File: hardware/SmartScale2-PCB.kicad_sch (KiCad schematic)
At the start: 43 parts, among them J1 Conn_ARM_JTAG_SWD_10, J2 USB_C_Receptacle_USB2.0_16P, J3 Conn_01x02, J4 Conn_01x06, J5 Conn_01x03_MountingPin, J6 Conn_01x04_MountingPin, Q1 MMBT4403, SW1 SW_Push_JTP-1130, U1 ESP32-C6-WROOM-1, U2 MCP73831-2-OT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

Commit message: PCB rough layout
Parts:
- removed Q1: MMBT4403, Package_TO_SOT_SMD:SOT-23, symbol Transistor_BJT:Q_PNP_EBC
- added J7: Conn_01x03, symbol Connector_Generic:Conn_01x03
- added Q1: MMBT4403, Package_TO_SOT_SMD:SOT-23, symbol Transistor_BJT:Q_PNP_BEC
- L2: footprint (none) -> Inductor_SMD:L_0805_2012Metric_Pad1.05x1.20mm_HandSolder
- R12: now not fitted
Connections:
- net A+: now also J4.4 (Pin_4); no longer J4.3 (Pin_3)
- net A-: now also J4.3 (Pin_3); no longer J4.4 (Pin_4)
- net B+: now also J4.6 (Pin_6); no longer J4.5 (Pin_5)
- net B-: now also J4.5 (Pin_5); no longer J4.6 (Pin_6)
- net GND: now also J7.1 (Pin_1)
- net T2: now reaches U1.26 (GPIO3/ADC1_CH3)
- net T2: now also J7.2 (Pin_2)
- net T1: now reaches U1.27 (GPIO2/ADC1_CH2)
- net T1: now also J7.3 (Pin_3)
- net Q1_E: now reaches JP1.1 (A), U3.1 (VSUP)
- net Q1_E: now also Q1.2 (E)
- net Q1_B: now reaches U3.2 (BASE)
- net Q1_B: now also Q1.1 (B)
- net Q1_C: now reaches L2.2, R6.1, U3.3 (AVDD)
- net Q1_C: now also Q1.3 (C)

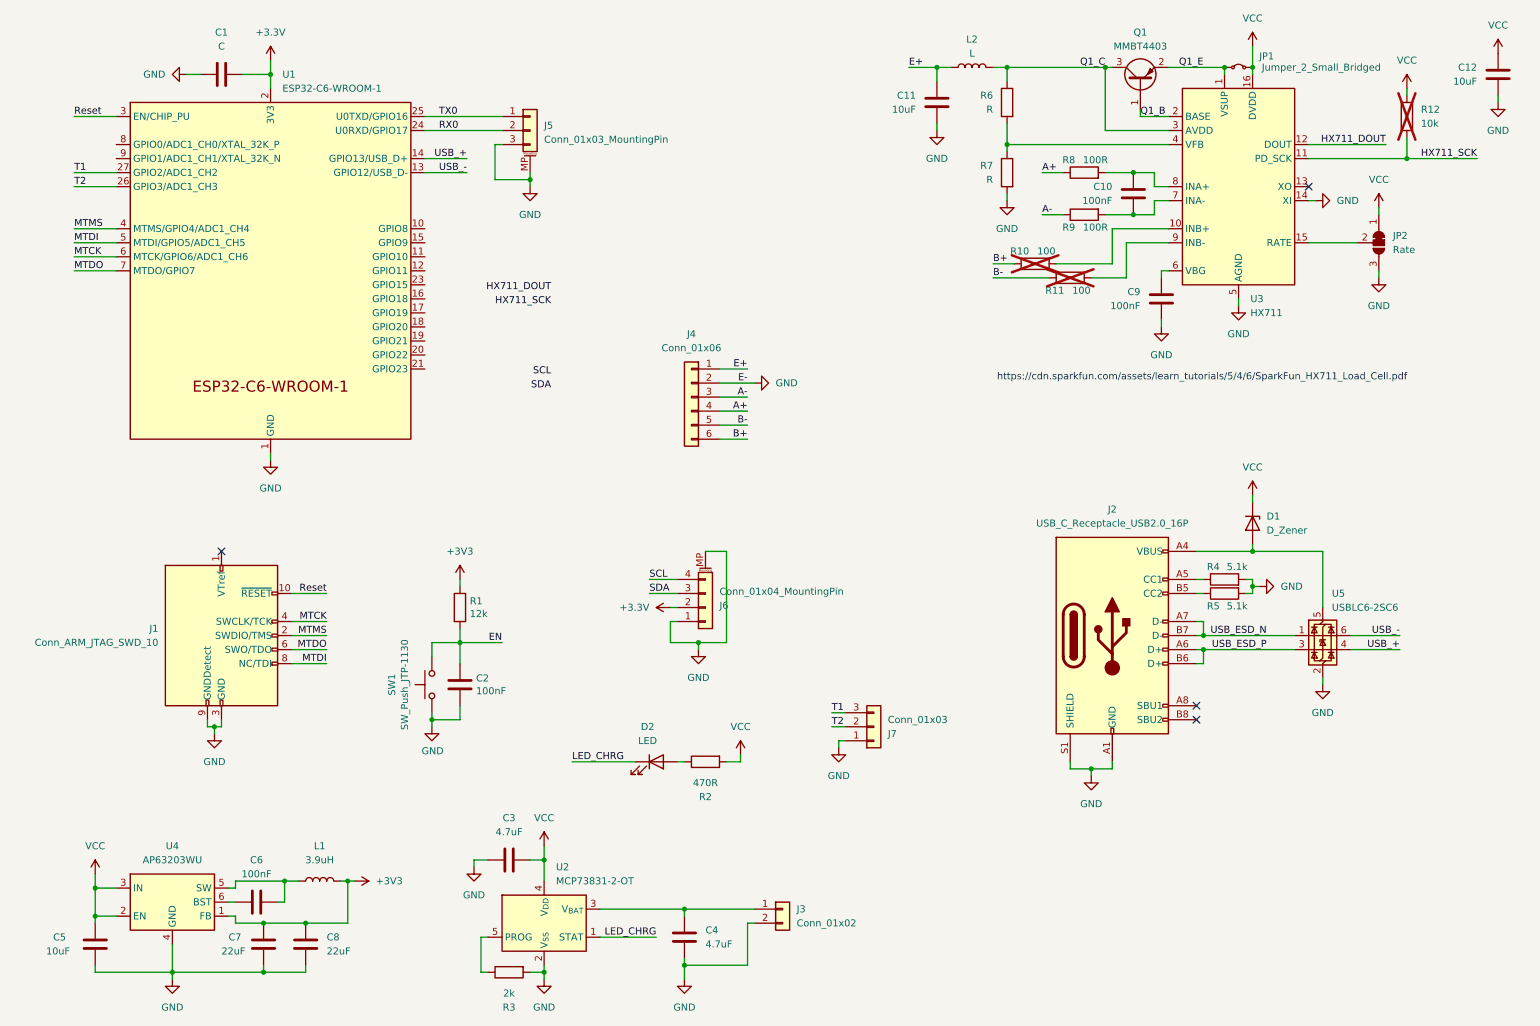
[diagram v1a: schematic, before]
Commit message: Add Touch IC, continue layout
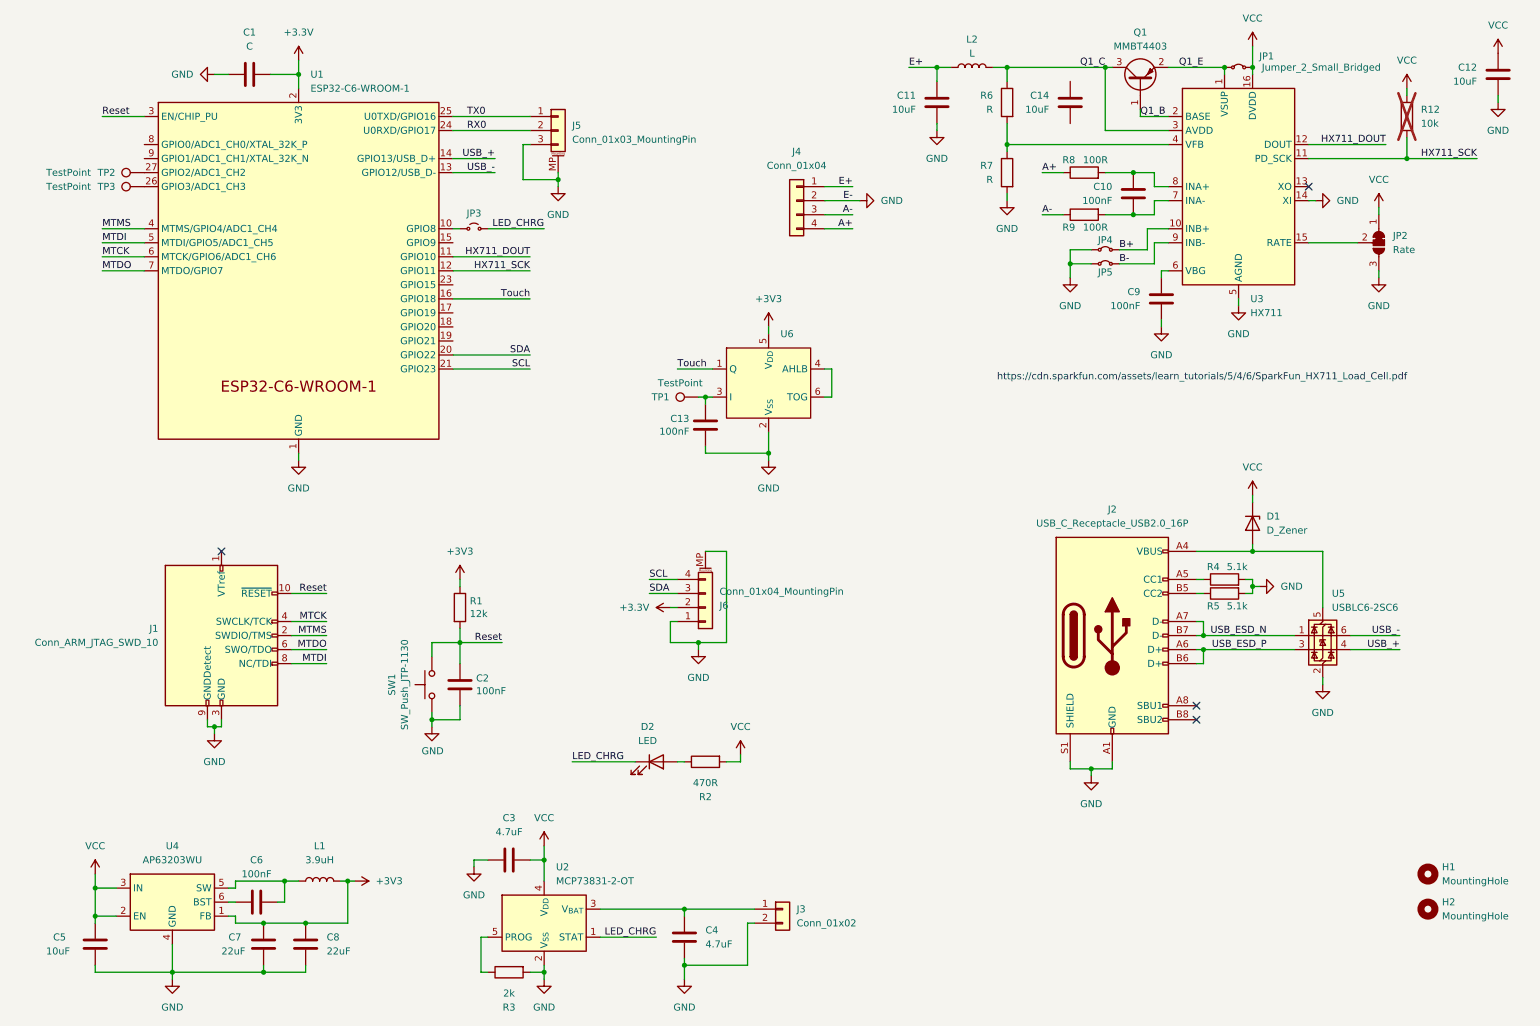
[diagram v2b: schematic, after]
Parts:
- removed J4: Conn_01x06, Connector_PinHeader_2.54mm:PinHeader_1x06_P2.54mm_Vertical, symbol Connector_Generic:Conn_01x06
- removed J7: Conn_01x03, symbol Connector_Generic:Conn_01x03
- removed R10, R11: 100, Resistor_SMD:R_0805_2012Metric_Pad1.20x1.40mm_HandSolder, symbol Device:R
- added C13: 100nF, Capacitor_SMD:C_0805_2012Metric_Pad1.18x1.45mm_HandSolder, symbol SmartScale-rescue:C-Device
- added C14: 10uF, Capacitor_SMD:C_0805_2012Metric_Pad1.18x1.45mm_HandSolder, symbol Device:C
- added H1, H2: MountingHole, MountingHole:MountingHole_3.2mm_M3_DIN965, symbol Mechanical:MountingHole
- added J4: Conn_01x04, Connector_PinSocket_2.54mm:PinSocket_1x04_P2.54mm_Vertical, symbol Connector_Generic:Conn_01x04
- added JP3: Jumper_2_Small_Open, Jumper:SolderJumper-2_P1.3mm_Open_RoundedPad1.0x1.5mm, symbol Jumper:Jumper_2_Small_Open
- added JP4, JP5: Jumper_2_Small_Bridged, Jumper:SolderJumper-2_P1.3mm_Bridged_RoundedPad1.0x1.5mm, symbol Jumper:Jumper_2_Small_Bridged
- added TP1: TestPoint, TestPoint:TestPoint_Loop_D2.50mm_Drill1.0mm, symbol Connector:TestPoint
- added TP2, TP3: TestPoint, TestPoint:TestPoint_Pad_D1.0mm, symbol Connector:TestPoint
- added U6: (no value), Package_TO_SOT_SMD:SOT-23-6, symbol _custom:TTP223-BA6
- D1: footprint (none) -> Diode_SMD:D_SOD-123
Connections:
- net EN is gone; now on net Reset: C2.1, R1.2, SW1.2
- net +3V3: now also U6.5 (V_{DD})
- net A+: now also J4.4 (Pin_4)
- net A-: now also J4.3 (Pin_3)
- net B+: now also U3.10 (INB+), JP4.2 (B)
- net B-: now also U3.9 (INB-), JP5.2 (B)
- net E+: now also J4.1 (Pin_1)
- net GND: now also C13.2, J4.2 (Pin_2), JP4.1 (A), JP5.1 (A), U6.2 (V_{SS})
- net HX711_DOUT: now also U1.11 (GPIO10)
- net HX711_SCK: now also U1.12 (GPIO11)
- net LED_CHRG: now also JP3.2 (B)
- net SCL: now also U1.21 (GPIO23)
- net SDA: now also U1.20 (GPIO22)
- net at U1.10 (GPIO8): now also JP3.1 (A)
- net Touch: now reaches U1.16 (GPIO18)
- net Touch: now also U6.1 (Q)
- net T1: no longer names the net of U1.27 (GPIO2/ADC1_CH2)
- net T1: now also TP2.1
- net T2: no longer names the net of U1.26 (GPIO3/ADC1_CH3)
- net T2: now also TP3.1
- new net: C13.1, TP1.1, U6.3 (I)
- new net: U6.4 (AHLB), U6.6 (TOG)
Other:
- moved on the sheet: C1, J5, U1

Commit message: Push from laptop
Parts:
- removed TP2: TestPoint, TestPoint:TestPoint_Pad_D1.0mm, symbol Connector:TestPoint
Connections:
- net +BATT: now reaches C4.1, J3.1 (Pin_1), U2.3 (V_{BAT})
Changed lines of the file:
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@@
 	(wire
 		(pts
+			(xy 132.08 173.99) (xy 132.08 176.53)
+		)
+		(stroke
+			(width 0)
+			(type default)
+		)
+	)
+	(wire
+		(pts
 			(xy 143.51 186.69) (xy 132.08 186.69)
 		)
@@
 	)
 	(symbol
-		(lib_id "Connector:TestPoint")
-		(at 34.29 43.18 90)
-		(unit 1)
-		(body_style 1)
-		(exclude_from_sim no)
-		(in_bom yes)
-		(on_board yes)
-		(in_pos_files yes)
-		(dnp no)
-		(property "Reference" "TP2"
-			(at 27.432 43.18 90)
-			(show_name no)
-			(do_not_autoplace no)
-			(effects
-				(font
-					(size 1.27 1.27)
-				)
-			)
-		)
-		(property "Value" "TestPoint"
-			(at 20.574 43.18 90)
-			(show_name no)
-			(do_not_autoplace no)
-			(effects
-				(font
-					(size 1.27 1.27)
-				)
-			)
-		)
-		(property "Footprint" "TestPoint:TestPoint_Pad_D1.0mm"
-			(at 34.29 38.1 0)
-			(hide yes)
-			(show_name no)
-			(do_not_autoplace no)
-			(effects
-				(font
-					(size 1.27 1.27)
-				)
-			)
-		)
-		(property "Datasheet" ""
-			(at 34.29 38.1 0)
-			(hide yes)
-			(show_name no)
-			(do_not_autoplace no)
-			(effects
-				(font
-					(size 1.27 1.27)
-				)
-			)
-		)
-		(property "Description" "test point"
-			(at 34.29 43.18 0)
-			(hide yes)
-			(show_name no)
-			(do_not_autoplace no)
-			(effects
-				(font
-					(size 1.27 1.27)
-				)
-			)
-		)
-		(pin "1"
-		)
-		(instances
-			(project "SmartScale2-PCB"
-				(path "/eb8fe25f-2338-48bc-9e7d-778edca2e81f"
-					(reference "TP2")
-					(unit 1)
-				)
-			)
-		)
-	)
-	(symbol
 		(lib_id "power:GND")
 		(at 106.68 189.23 0)
@@
 					(unit 1)
 				)
+			)
+		)
+	)
+	(symbol
+		(lib_id "power:+BATT")
+		(at 132.08 173.99 0)
+		(unit 1)
+		(body_style 1)
+		(exclude_from_sim no)
+		(in_bom yes)
+		(on_board yes)
+		(in_pos_files yes)
+		(dnp no)
+		(fields_autoplaced yes)
+		(property "Reference" "#PWR031"
+			(at 132.08 177.8 0)
+			(hide yes)
+			(show_name no)
+			(do_not_autoplace no)
+			(effects
+				(font
+					(size 1.27 1.27)
+				)
+			)
+		)
+		(property "Value" "+BATT"
+			(at 132.08 168.91 0)
+			(show_name no)
+			(do_not_autoplace no)
+			(effects
+				(font
+					(size 1.27 1.27)
+				)
+			)
+		)
+		(property "Footprint" ""
+			(at 132.08 173.99 0)
+			(hide yes)
+			(show_name no)
+			(do_not_autoplace no)
+			(effects
+				(font
+					(size 1.27 1.27)
+				)
+			)
+		)
+		(property "Datasheet" ""
+			(at 132.08 173.99 0)
+			(hide yes)
+			(show_name no)
+			(do_not_autoplace no)
+			(effects
+				(font
+					(size 1.27 1.27)
+				)
+			)
+		)
+		(property "Description" "Power symbol creates a global label with name \"+BATT\""
+			(at 132.08 173.99 0)
+			(hide yes)
+			(show_name no)
+			(do_not_autoplace no)
+			(effects
+				(font
+					(size 1.27 1.27)
+				)
+			)
+		)
+		(pin "1"
+		)
+		(instances
+			(project "SmartScale2-PCB"
+				(path "/eb8fe25f-2338-48bc-9e7d-778edca2e81f"
+					(reference "#PWR031")
+					(unit 1)
+				)

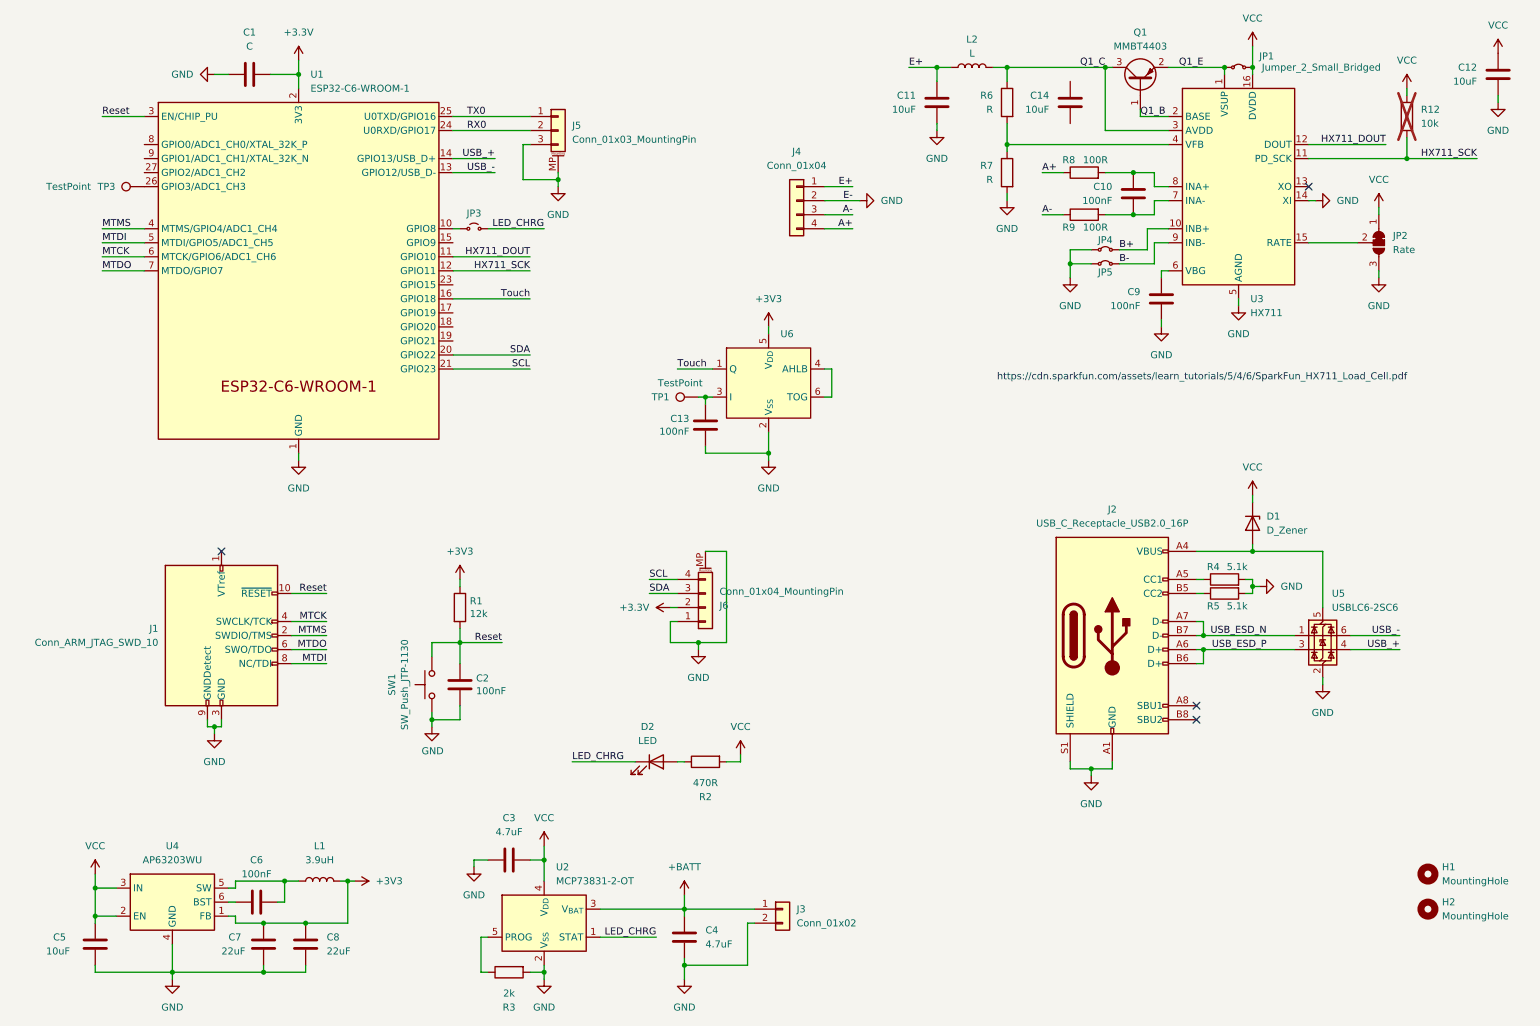
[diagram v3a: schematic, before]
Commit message: Finish PCB layout
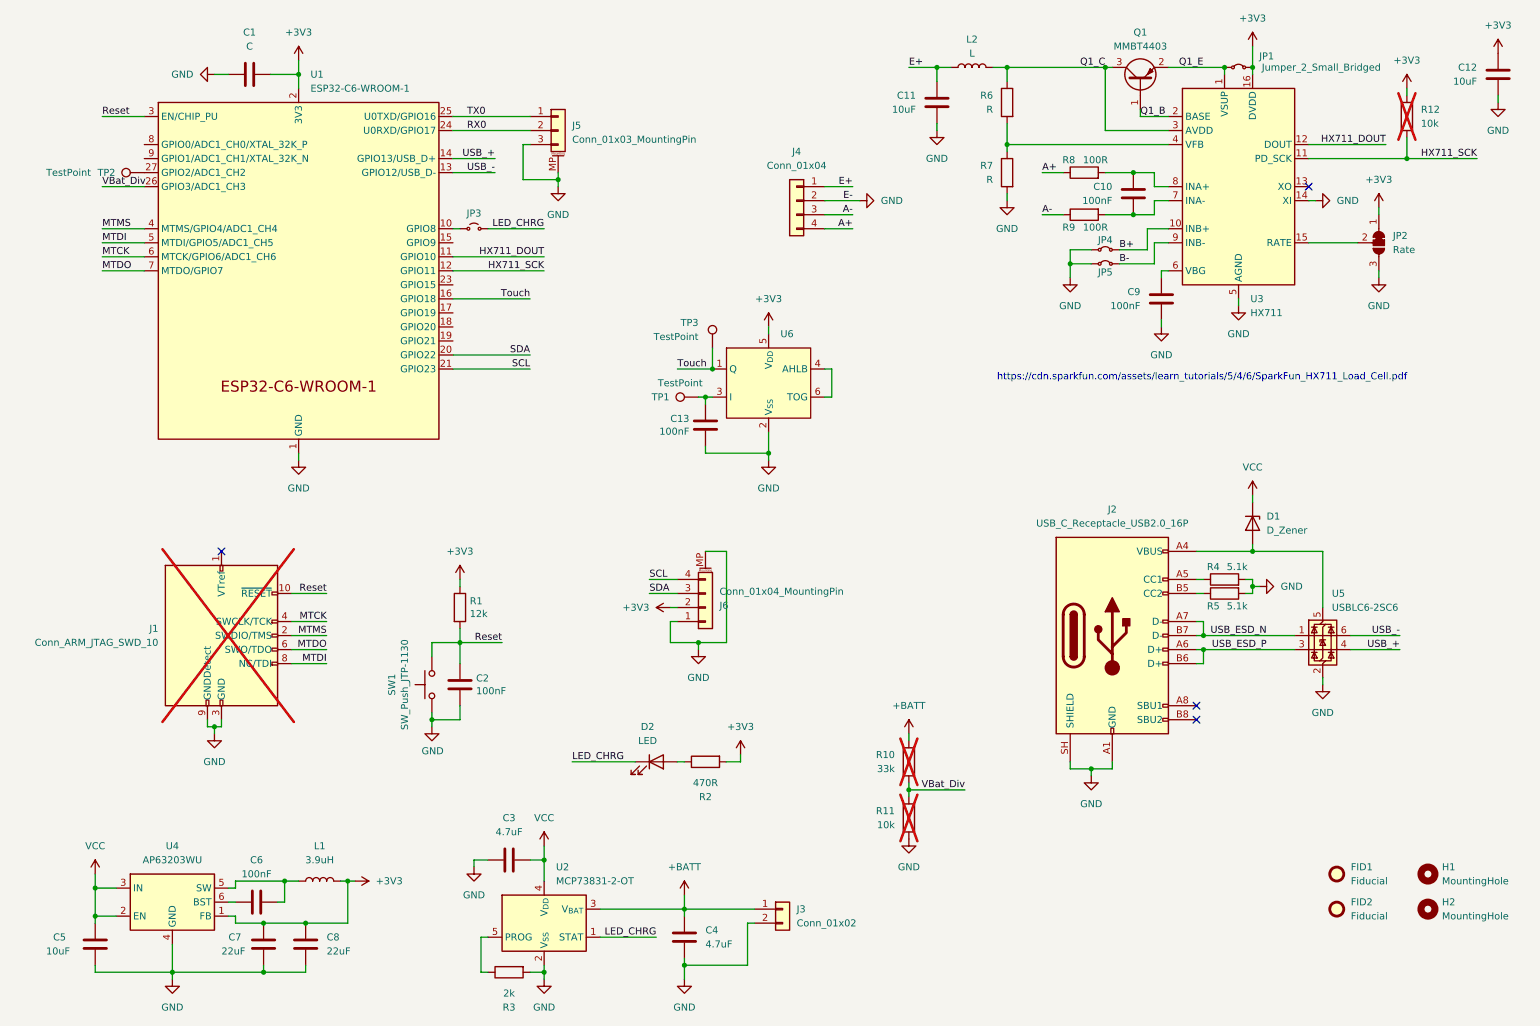
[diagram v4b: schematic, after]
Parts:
- removed C14: 10uF, Capacitor_SMD:C_0805_2012Metric_Pad1.18x1.45mm_HandSolder, symbol Device:C
- added FID1, FID2: Fiducial, Fiducial:Fiducial_0.5mm_Mask1.5mm, symbol Mechanical:Fiducial
- added R10: 33k, Resistor_SMD:R_0805_2012Metric_Pad1.20x1.40mm_HandSolder, symbol Device:R
- added R11: 10k, Resistor_SMD:R_0805_2012Metric_Pad1.20x1.40mm_HandSolder, symbol Device:R
- added TP2: TestPoint, TestPoint:TestPoint_Pad_D1.0mm, symbol Connector:TestPoint
- J1: now not fitted
- J4, JP1, JP3, JP4, JP5, TP3: now left out of the parts list
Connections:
- net +3.3V is gone; now on net +3V3: C1.2, J6.2 (Pin_2), U1.2 (3V3)
- net +3V3: now also C12.1, JP1.2 (B), JP2.1 (A), R12.1, R2.2, U3.16 (DVDD)
- net +BATT: now also R10.1
- net GND: now also J2.SH (SHIELD), R11.2; no longer J2.S1 (SHIELD)
- net Touch: now also TP3.1
- net VCC: no longer C12.1, JP1.2 (B), JP2.1 (A), R12.1, R2.2, U3.16 (DVDD)
- net VBat_Div: now reaches U1.26 (GPIO3/ADC1_CH3)
- net VBat_Div: now also R10.2, R11.1; no longer TP3.1
- net at U1.27 (GPIO2/ADC1_CH2): now also TP2.1
